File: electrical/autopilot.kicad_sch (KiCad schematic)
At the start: 5 parts

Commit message: Interim check-in
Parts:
- removed CWS_SW: SW_Push, symbol Switch:SW_Push
- removed GSA28_YAW: ~, symbol flyerx:Garmin_GSA28
- added PITCH_TRIM: T3, symbol flyerx:Ray_Allen_T2/T3
- added PITP1: DTM6P, symbol Connector:Conn_01x06_Socket
- added PITR1: DTM6R, symbol Connector:Conn_01x06_Pin
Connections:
- net CAN_HI_ROLL_IN is gone; now on net CAN_HI_PITCH_OUT: GSA28_ROLL.P281_1 (CAN-H)
- net CAN_LO_ROLL_IN is gone; now on net CAN_LO_PITCH_OUT: GSA28_ROLL.P281_2 (CAN-L)
- net CAN_HI_PITCH_OUT: now also GSA28_PITCH.P281_13 (TRIM_OUT_1), PITR1.1 (Pin_1), PITR1.4 (Pin_4)
- net CAN_LO_PITCH_OUT: now also GSA28_PITCH.P281_14 (TRIM_OUT_2), PITR1.2 (Pin_2), PITR1.5 (Pin_5)
- net CWS_ON: now reaches GSA28_PITCH.P281_15 (CWS-DISCONNECT), GSA28_ROLL.P281_15 (CWS-DISCONNECT)
- net PITCH_TRIM1: now reaches GSA28_PITCH.P281_11 (TRIM_IN_1)
- net PITCH_TRIM2: now reaches GSA28_PITCH.P281_12 (TRIM_IN_2)
- new net: PITCH_TRIM.B (LOW), PITP1.3 (Pin_3)
- new net: PITCH_TRIM.G (SENSE), PITP1.2 (Pin_2)
- new net: PITCH_TRIM.GY (TRIM2), PITP1.5 (Pin_5)
- new net: PITCH_TRIM.O (+5V), PITP1.1 (Pin_1)
- new net: PITCH_TRIM.W (TRIM1), PITP1.4 (Pin_4)
- new net PITCH_TRIM_LO: PITR1.3 (Pin_3)
- no-connect marks 29 -> 21
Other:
- note added: "POS is 3 Conductor 22/24 AWG Trim1/2 is 2 Conductor 20 AWG"

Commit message: Interim check-in
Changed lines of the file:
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@@
+	(wire
+		(pts
+			(xy 57.15 107.95) (xy 73.66 107.95)
+		)
+		(stroke
+			(width 0)
+			(type dash)
+		)
+	)
 	(wire
 		(pts
@@
 					(unit 1)
 				)
+			)
+		)
+	)
+	(symbol
+		(lib_id "power:GNDS")
+		(at 57.15 107.95 270)
+		(unit 1)
+		(exclude_from_sim no)
+		(in_bom yes)
+		(on_board yes)
+		(dnp no)
+		(fields_autoplaced yes)
+		(property "Reference" "#PWR054"
+			(at 50.8 107.95 0)
+			(effects
+				(font
+					(size 1.27 1.27)
+				)
+				(hide yes)
+			)
+		)
+		(property "Value" "GNDS"
+			(at 52.07 107.95 0)
+			(effects
+				(font
+					(size 1.27 1.27)
+				)
+				(hide yes)
+			)
+		)
+		(property "Footprint" ""
+			(at 57.15 107.95 0)
+			(effects
+				(font
+					(size 1.27 1.27)
+				)
+				(hide yes)
+			)
+		)
+		(property "Datasheet" ""
+			(at 57.15 107.95 0)
+			(effects
+				(font
+					(size 1.27 1.27)
+				)
+				(hide yes)
+			)
+		)
+		(property "Description" "Power symbol creates a global label with name \"GNDS\" , signal ground"
+			(at 57.15 107.95 0)
+			(effects
+				(font
+					(size 1.27 1.27)
+				)
+				(hide yes)
+			)
+		)
+		(pin "1"
+		)
+		(instances
+			(project "electrical"
+				(path "/e8ec215a-dbe2-4eba-a577-e50a0a128049/bd38efb0-077c-4462-9d19-e07b49d43233"
+					(reference "#PWR054")
+					(unit 1)
+				)

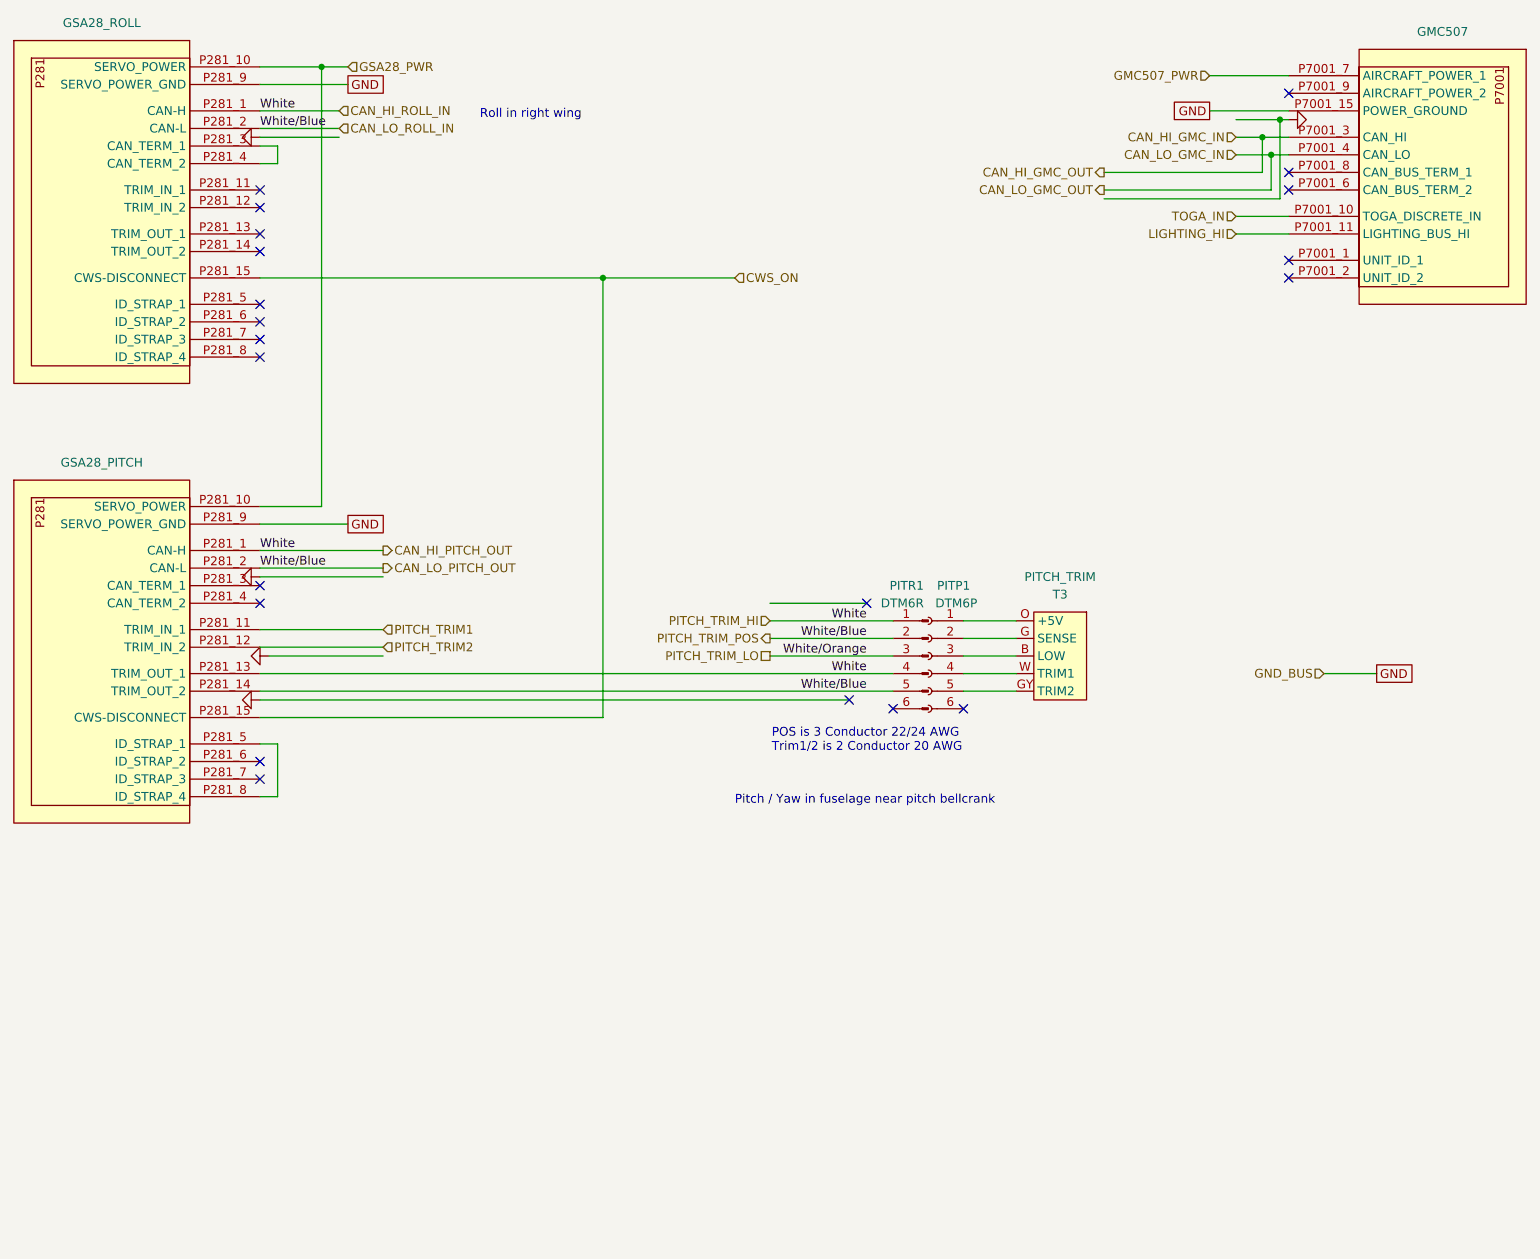
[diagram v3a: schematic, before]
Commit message: Went through and changed a lot from discussions and tradeoffs. Added GTX 330, rmemoved Connext from GDU and added to GPS 175 from GDL 52. Added relay for smoke and to not use GAD 27. Added Tach sensor for SureFly. Added carb heat. Added connectors to run panel disconnected.
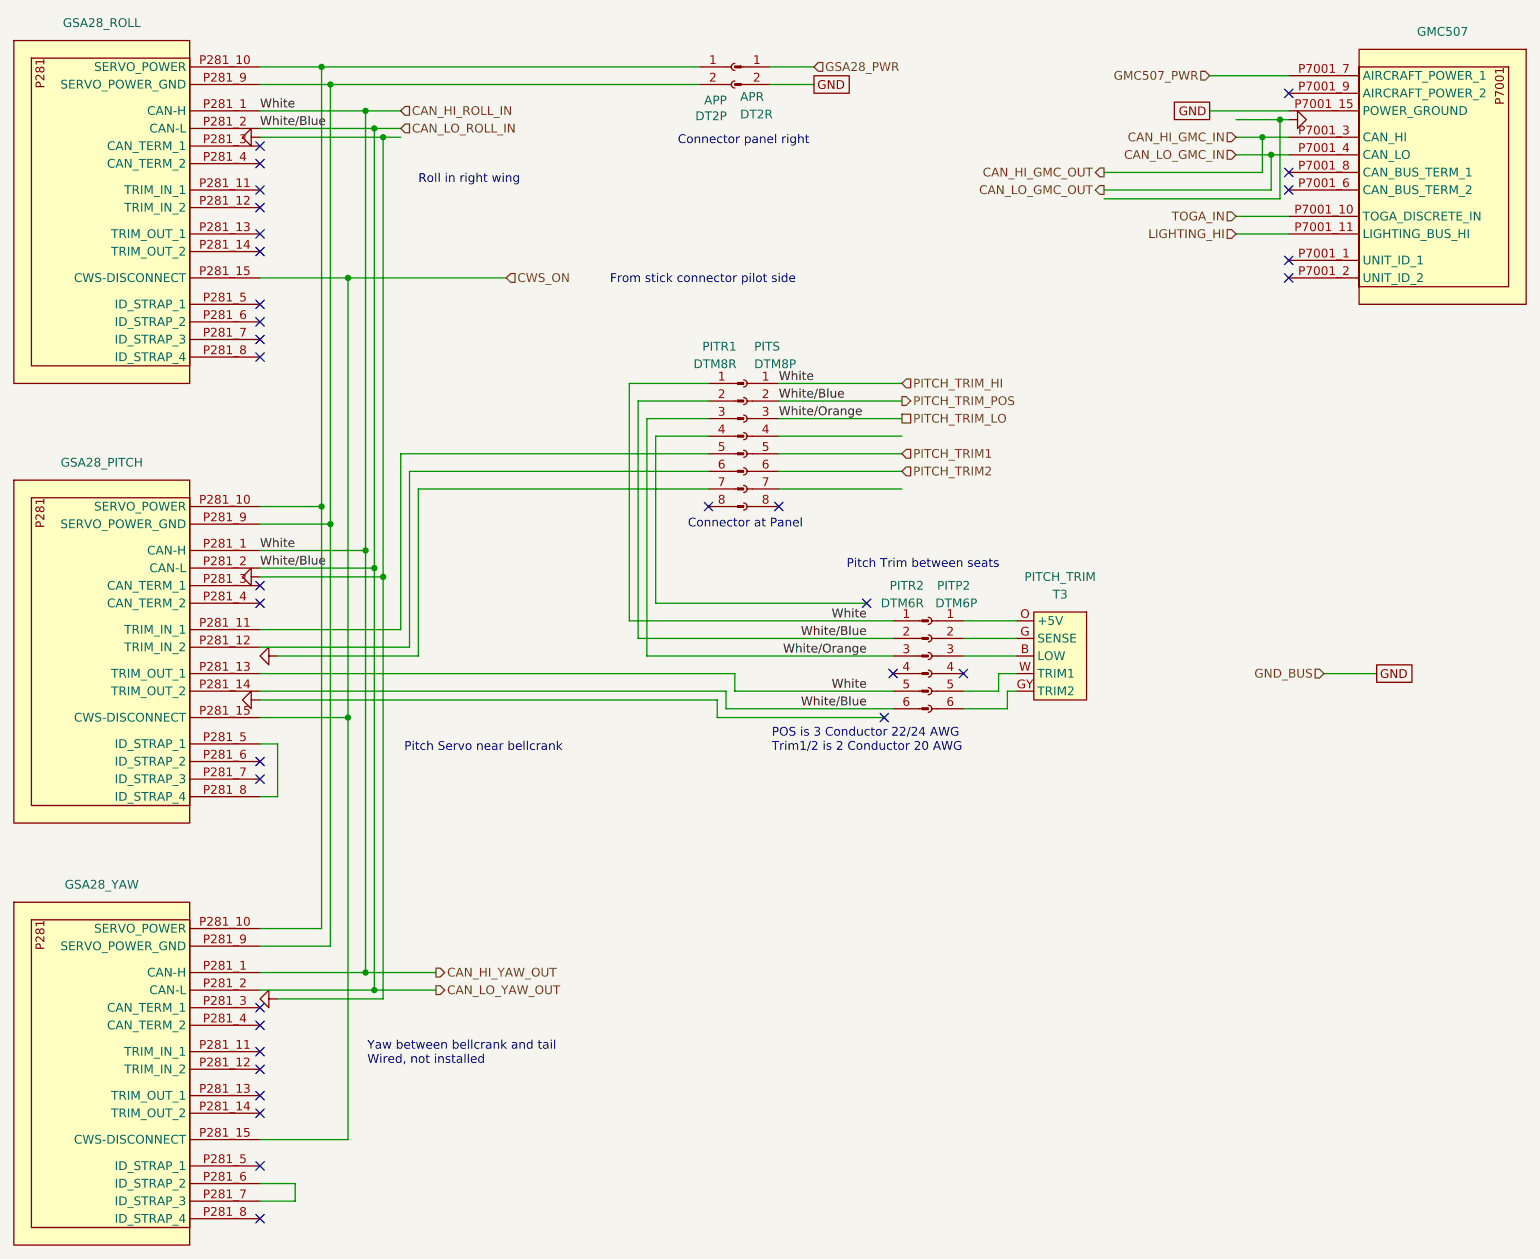
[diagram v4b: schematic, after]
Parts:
- added APP: DT2P, symbol Connector:Conn_01x02_Socket
- added APR: DT2R, symbol Connector:Conn_01x02_Pin
- added GSA28_YAW: ~, symbol flyerx:Garmin_GSA28
- added PITR1: DTM8R, symbol Connector:Conn_01x08_Pin
- added PITS: DTM8P, symbol Connector:Conn_01x08_Socket
- renumbered PITP1 to PITP2, PITR1 to PITR2
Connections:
- net CWS_ON: now also GSA28_YAW.P281_15 (CWS-DISCONNECT)
- net GND: now also APR.2 (Pin_2); no longer GSA28_PITCH.P281_9 (SERVO_POWER_GND), GSA28_ROLL.P281_9 (SERVO_POWER_GND)
- net GNDS: now also PITR1.7 (Pin_7)
- net GSA28_PWR: now also APR.1 (Pin_1); no longer GSA28_PITCH.P281_10 (SERVO_POWER), GSA28_ROLL.P281_10 (SERVO_POWER)
- net PITCH_TRIM1: now also PITS.5 (Pin_5); no longer GSA28_PITCH.P281_11 (TRIM_IN_1)
- net PITCH_TRIM2: now also PITS.6 (Pin_6); no longer GSA28_PITCH.P281_12 (TRIM_IN_2)
- net PITCH_TRIM_LO: now also PITR1.3 (Pin_3), PITS.3 (Pin_3)
- net CAN_LO_ROLL_IN: now reaches PITR2.6 (Pin_6)
- net CAN_LO_ROLL_IN: now also GSA28_PITCH.P281_14 (TRIM_OUT_2), GSA28_PITCH.P281_2 (CAN-L), GSA28_ROLL.P281_2 (CAN-L), PITR2.2 (Pin_2), GSA28_YAW.P281_2 (CAN-L), PITR1.2 (Pin_2), PITS.2 (Pin_2)
- net at PITCH_TRIM.GY (TRIM2): now also PITP2.6 (Pin_6); no longer PITP2.5 (Pin_5)
- net at PITCH_TRIM.W (TRIM1): now also PITP2.5 (Pin_5); no longer PITP2.4 (Pin_4)
- net at GSA28_ROLL.P281_3 (CAN_TERM_1): no longer GSA28_ROLL.P281_4 (CAN_TERM_2)
- net CAN_HI_PITCH_OUT renamed CAN_HI_ROLL_IN
- net CAN_HI_ROLL_IN: now also PITR2.5 (Pin_5), GSA28_YAW.P281_1 (CAN-H), PITR1.1 (Pin_1), PITS.1 (Pin_1); no longer PITR2.4 (Pin_4)
- removed net CAN_LO_PITCH_OUT: GSA28_PITCH.P281_14 (TRIM_OUT_2), GSA28_PITCH.P281_2 (CAN-L), GSA28_ROLL.P281_2 (CAN-L), PITR2.2 (Pin_2), PITR2.5 (Pin_5)
- new net: APP.1 (Pin_1), GSA28_PITCH.P281_10 (SERVO_POWER), GSA28_ROLL.P281_10 (SERVO_POWER), GSA28_YAW.P281_10 (SERVO_POWER)
- new net: GSA28_YAW.P281_6 (ID_STRAP_2), GSA28_YAW.P281_7 (ID_STRAP_3)
- new net: APP.2 (Pin_2), GSA28_PITCH.P281_9 (SERVO_POWER_GND), GSA28_ROLL.P281_9 (SERVO_POWER_GND), GSA28_YAW.P281_9 (SERVO_POWER_GND)
- new net: GSA28_PITCH.P281_11 (TRIM_IN_1), PITR1.5 (Pin_5)
- new net: GSA28_PITCH.P281_12 (TRIM_IN_2), PITR1.6 (Pin_6)
- no-connect marks 21 -> 33
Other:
- note added: "Connector at Panel"
- note added: "Connector panel right"
- note added: "From stick connector pilot side"
- note added: "Pitch Servo near bellcrank"
- note added: "Pitch Trim between seats"
- note added: "Yaw between bellcrank and tail Wired, not installed"
- note removed: "Pitch / Yaw in fuselage near pitch bellcrank"

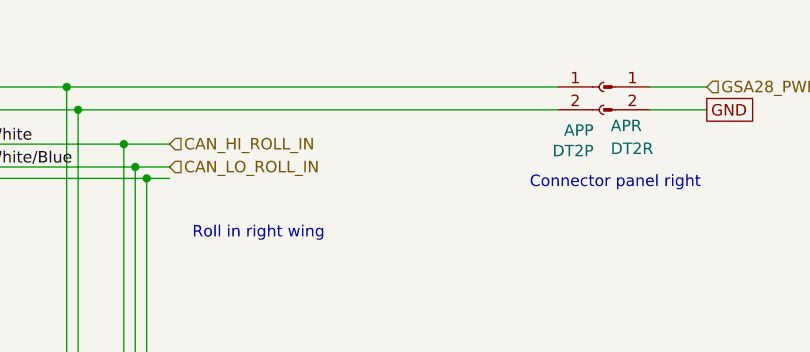
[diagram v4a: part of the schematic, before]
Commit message: Added AWG wires.
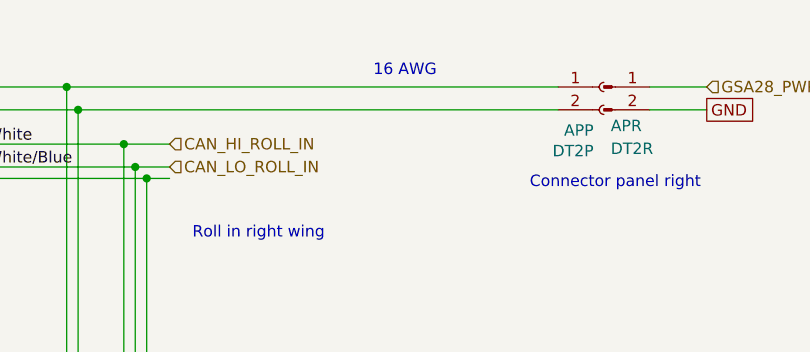
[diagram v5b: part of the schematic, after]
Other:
- note added: "16 AWG"
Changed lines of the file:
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@@
 		(title "Autopilot")
 		(date "2025-12-24")
-		(rev "1.2")
+		(rev "1.2.1")
 		(company "N877RV")
 	)
@@
 		(effects
 			(font
+				(size 1.27 1.27)
+			)
+		)
+	)
+	(text "16 AWG"
+		(exclude_from_sim no)
+		(at 102.362 21.082 0)
+		(effects
+			(font

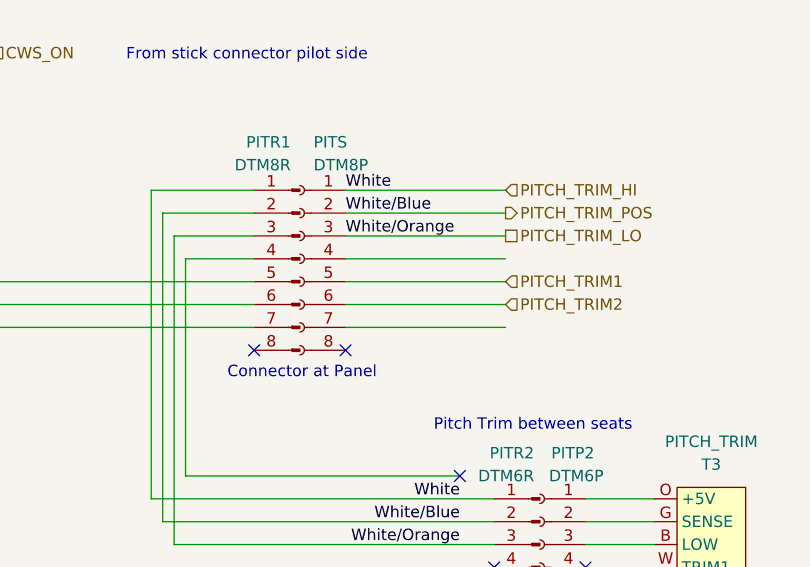
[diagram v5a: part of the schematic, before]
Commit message: Fixed can hi pin on GTR 20. Changed how ACX-BT wires with low vs. shield. Added pitch trim colors. Removed pitch trim ground going to flaps ground. Removed extra connector on GDL 52 and changed to 4 wire shielded instead of two 2 wire shielded.
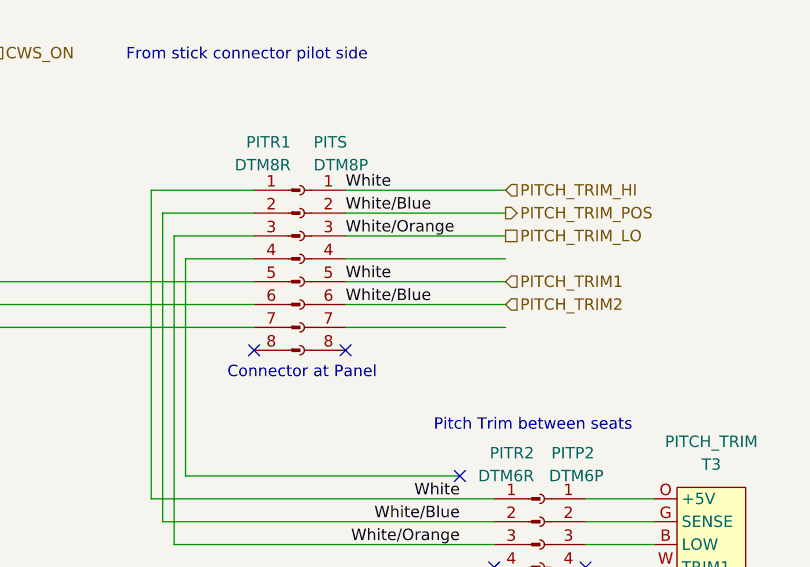
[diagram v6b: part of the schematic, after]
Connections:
- net PITCH_TRIM1 is gone; now on net CAN_HI_ROLL_IN: PITS.5 (Pin_5)
- net PITCH_TRIM2 is gone; now on net CAN_LO_ROLL_IN: PITS.6 (Pin_6)
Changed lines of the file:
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@@
 	(title_block
 		(title "Autopilot")
-		(date "2025-12-24")
-		(rev "1.2.1")
+		(date "2026-01-13")
+		(rev "1.2.11")
 		(company "N877RV")
 	)
@@
 	)
 	(label "White"
+		(at 130.81 78.74 0)
+		(effects
+			(font
+				(size 1.27 1.27)
+			)
+			(justify left bottom)
+		)
+	)
+	(label "White"
 		(at 55.88 29.21 0)
 		(effects
@@
 		)
 	)
+	(label "White{slash}Blue"
+		(at 130.81 81.28 0)
+		(effects
+			(font
+				(size 1.27 1.27)
+			)
+			(justify left bottom)
+		)
+	)

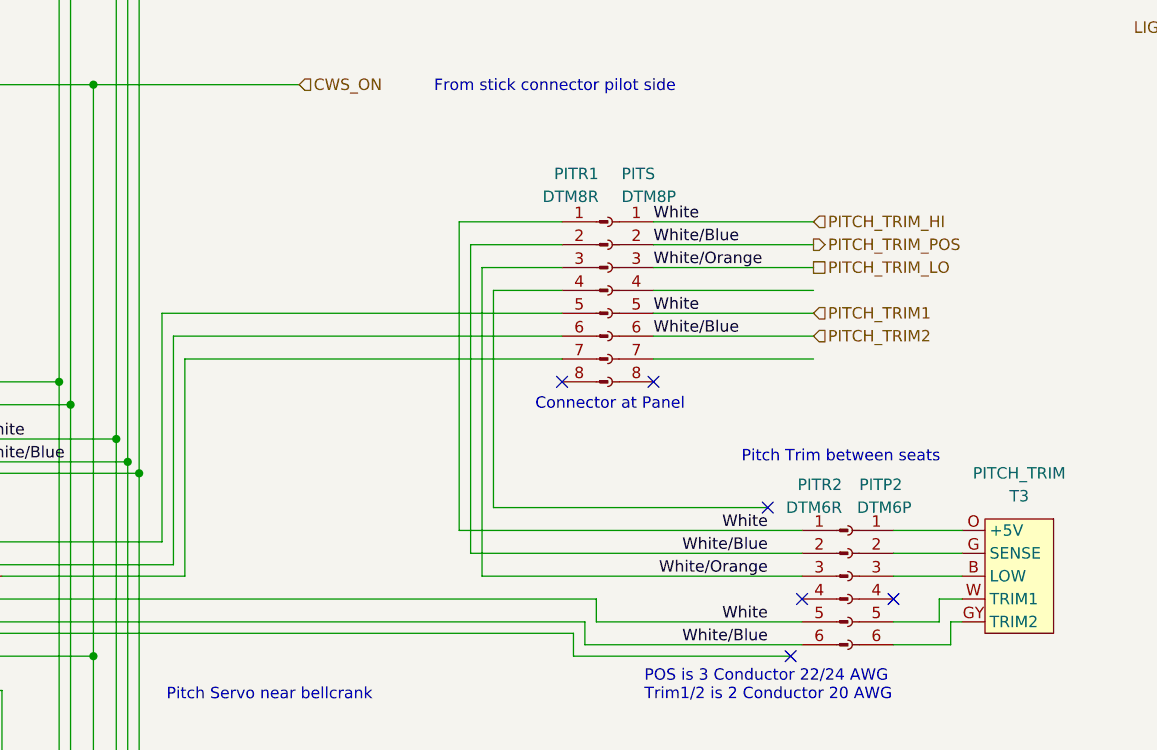
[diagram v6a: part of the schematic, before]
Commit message: Split Pitch Trim POS to go straight into connector. Changed colors on CO monitor to match what cable had. Changed colors of stick after father changed buttons.
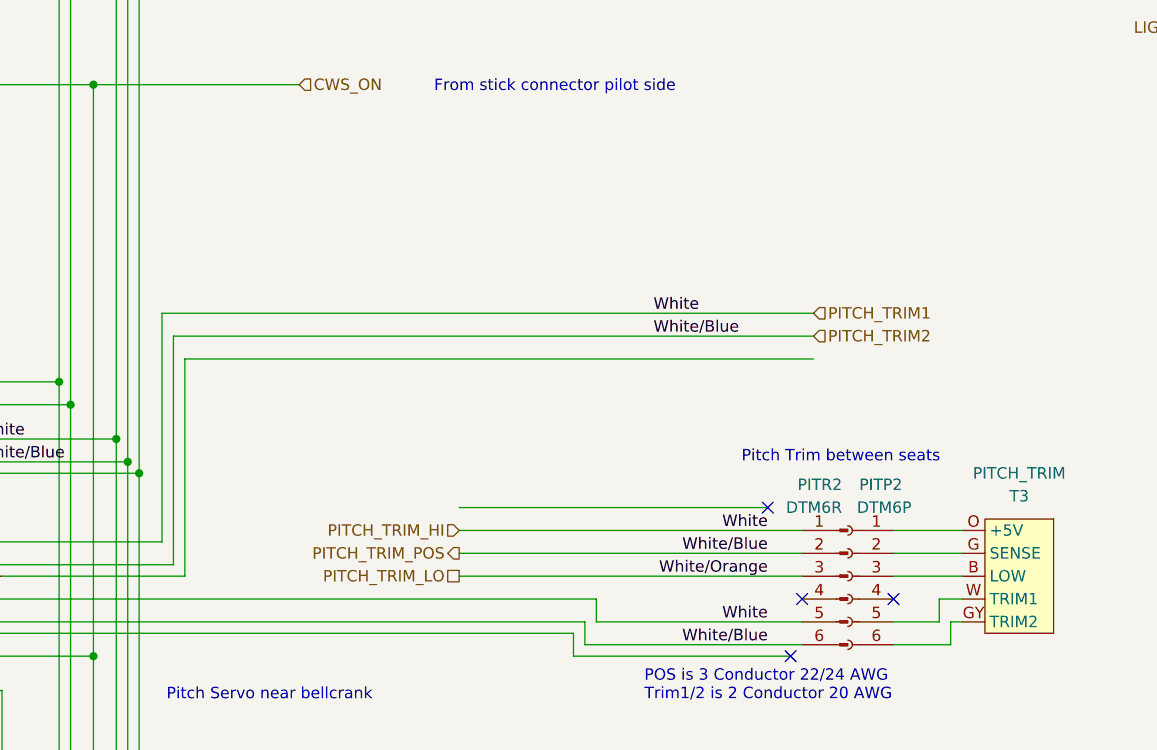
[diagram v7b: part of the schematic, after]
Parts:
- removed PITR1: DTM8R, symbol Connector:Conn_01x08_Pin
- removed PITS: DTM8P, symbol Connector:Conn_01x08_Socket
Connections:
- net CAN_HI_ROLL_IN: now also GSA28_PITCH.P281_11 (TRIM_IN_1)
- net CAN_LO_ROLL_IN: now also GSA28_PITCH.P281_12 (TRIM_IN_2)
- no-connect marks 33 -> 31
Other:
- note removed: "Connector at Panel"
